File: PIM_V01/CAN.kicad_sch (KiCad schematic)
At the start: 46 parts, among them U4 MCP2562FDT-E/SN, U5 MCP2562FDT-E/SN

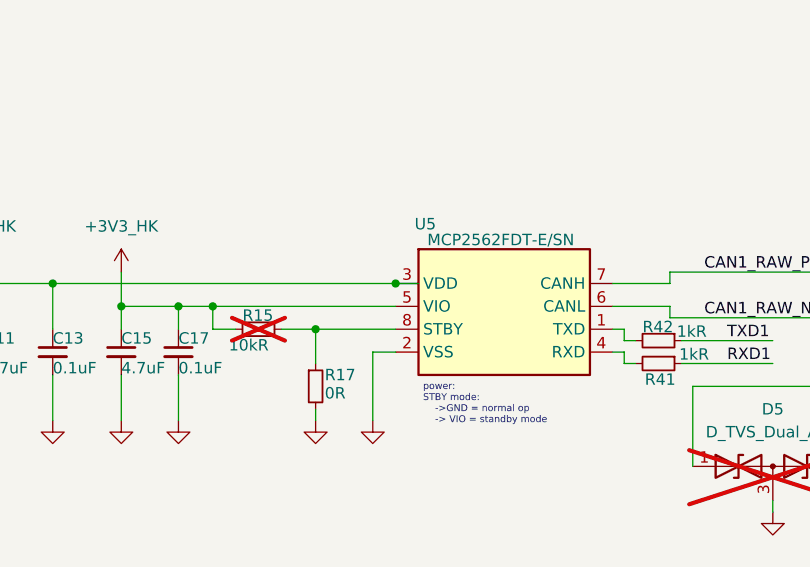
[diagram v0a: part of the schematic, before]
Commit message: updated schematic to include FRAM. Ben to review soon'
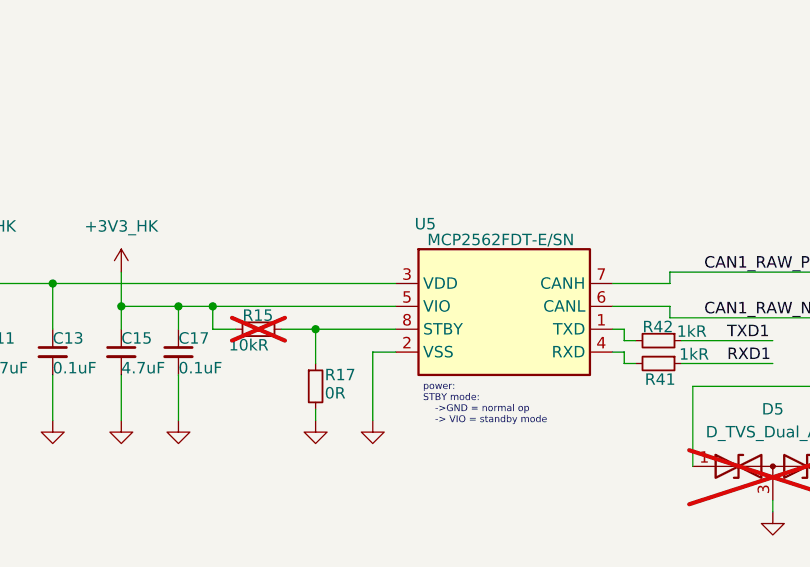
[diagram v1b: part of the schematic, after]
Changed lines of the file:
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@@
-	)
-	(junction
-		(at 186.69 156.21)
-		(diameter 0)
-		(color 0 0 0 0)
 	)
 	(junction
@@
 		)
 		(stroke
-			(width 0)
-			(type default)
-		)
-	)
-	(wire
-		(pts
-			(xy 189.23 156.21) (xy 186.69 156.21)
-		)
-		(stroke

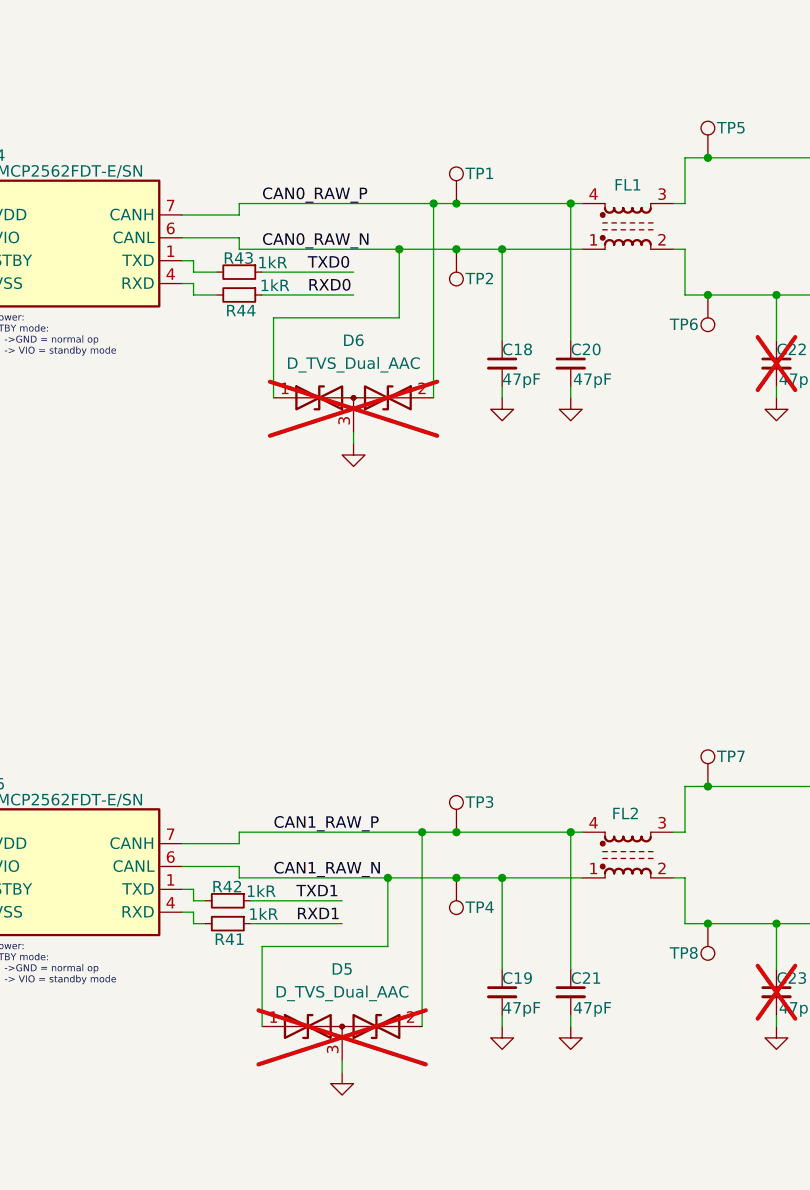
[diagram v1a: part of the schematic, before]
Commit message: minor updates to sch, bigger updates to pcb, after this push i am moving to double sided pcb for space optimisation
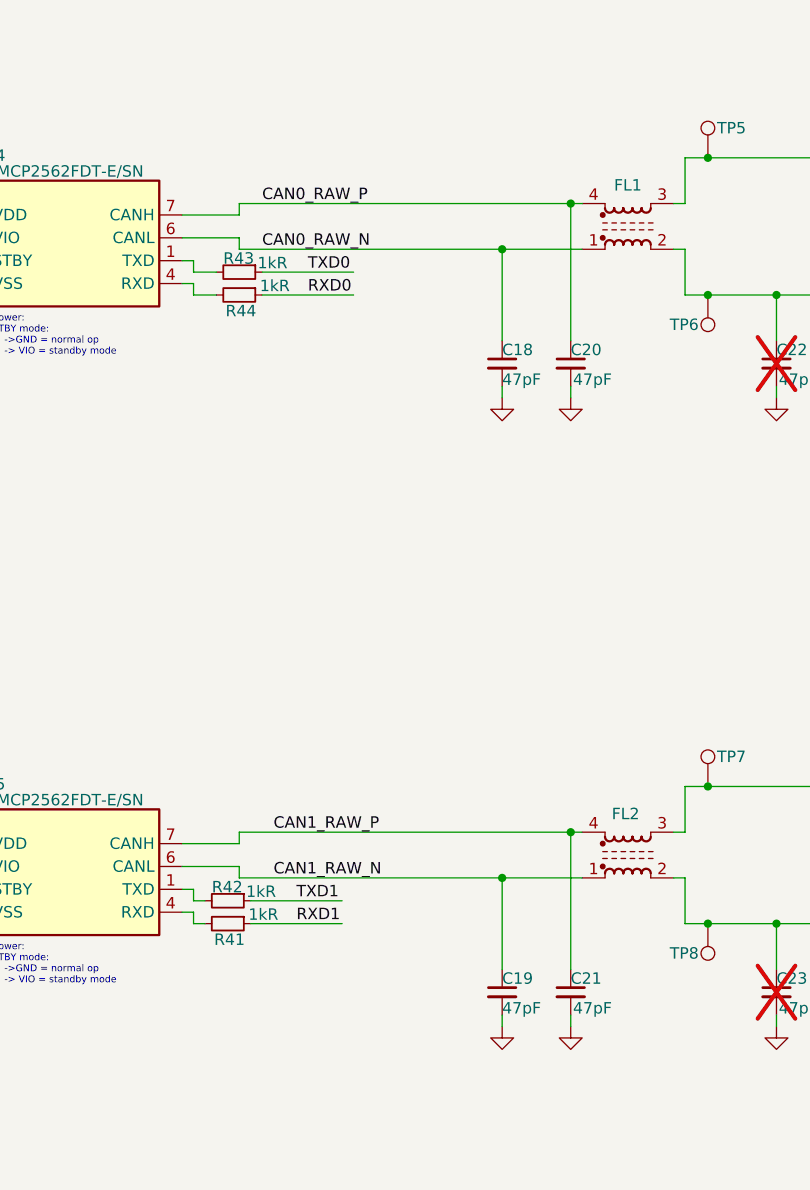
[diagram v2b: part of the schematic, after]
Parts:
- removed D5, D6: D_TVS_Dual_AAC, Package_TO_SOT_SMD:SOT-23-3, symbol Device:D_TVS_Dual_AAC
- removed TP1, TP2, TP3, TP4: TestPoint, TestPoint:TestPoint_Keystone_5000-5004_Miniature, symbol Connector:TestPoint

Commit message: ben to review, added mounting holes and finished the rest of the layout; also labelled more of the pinouts and added leds and tps
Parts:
- TP5, TP6, TP7, TP8: footprint TestPoint:TestPoint_Keystone_5000-5004_Miniature -> TestPoint:TestPoint_Pad_D1.0mm
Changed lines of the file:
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@@
 			)
 		)
-		(property "Footprint" "TestPoint:TestPoint_Keystone_5000-5004_Miniature"
+		(property "Footprint" "TestPoint:TestPoint_Pad_D1.0mm"
 			(at 274.32 149.86 0)
 			(effects
@@
 			)
 		)
-		(property "Footprint" "TestPoint:TestPoint_Keystone_5000-5004_Miniature"
+		(property "Footprint" "TestPoint:TestPoint_Pad_D1.0mm"
 			(at 264.16 165.1 0)
 			(effects
@@
 			)
 		)
-		(property "Footprint" "TestPoint:TestPoint_Keystone_5000-5004_Miniature"
+		(property "Footprint" "TestPoint:TestPoint_Pad_D1.0mm"
 			(at 264.16 95.25 0)
 			(effects
@@
 			)
 		)
-		(property "Footprint" "TestPoint:TestPoint_Keystone_5000-5004_Miniature"
+		(property "Footprint" "TestPoint:TestPoint_Pad_D1.0mm"
 			(at 274.32 80.01 0)
 			(effects
